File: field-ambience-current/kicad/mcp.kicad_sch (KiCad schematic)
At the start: 41 parts, among them SW1 Cell 1 (2u Choc V2 Hot-Swap), SW10 Modifier CLEAR (12x12x7.3 SMD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, SW2 Cell 2 (2u Choc V2 Hot-Swap), SW3 Cell 3 (2u Choc V2 Hot-Swap), SW4 Cell 4 (2u Choc V2 Hot-Swap), SW5 Cell 5 (2u Choc V2 Hot-Swap), SW6 Modifier SHIFT (12x12x7.3 SMD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, SW7 Modifier HOLD (12x12x7.3 SMD-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, SW8 Modifier DRONE (12x12x7.3 SMD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, SW9 Modifier GENERATE (12x12x7.3 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

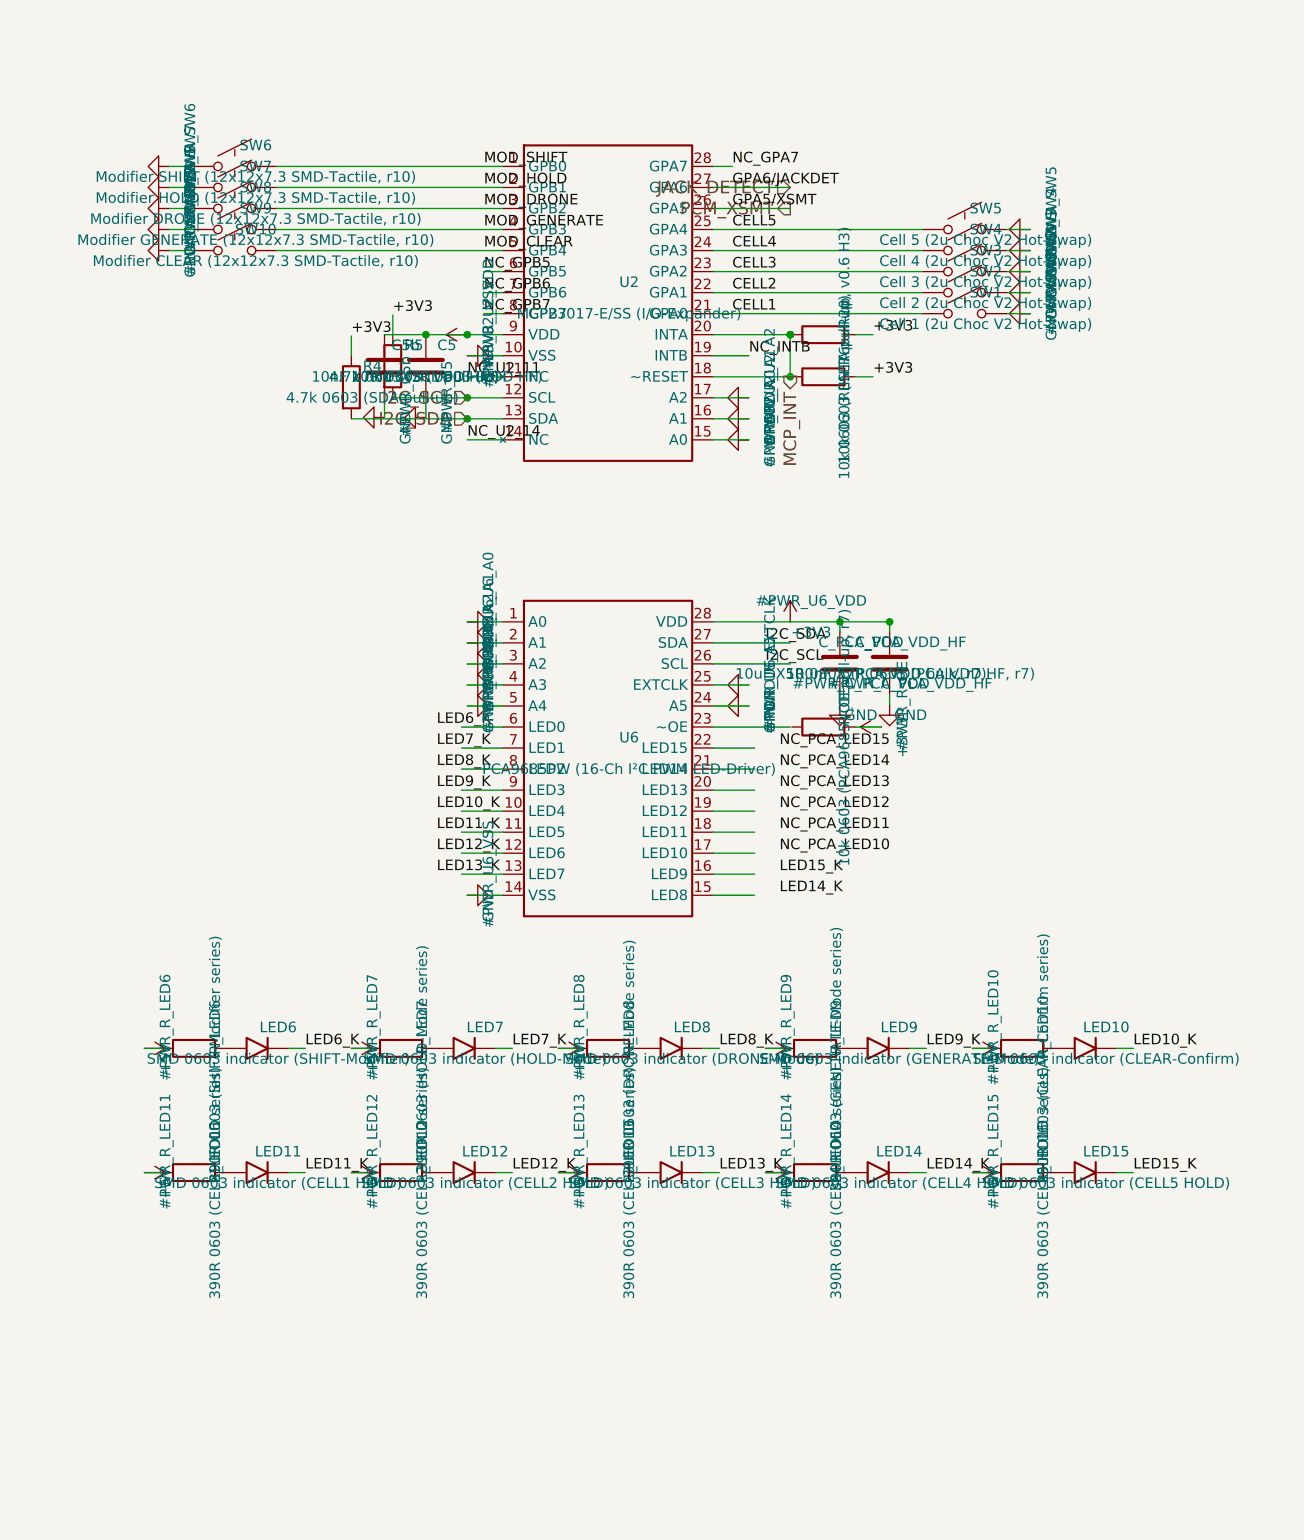
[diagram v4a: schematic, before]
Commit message: pcb(gen): r12-Sense + r9-Battery — KiCad-Generator vervollständigt
Zweite + dritte Hälfte von r10-B9/r7-B3. Bringt Generator vollständig in
Sync mit allen SPEC-Revisionen r9 (Battery-Add), r12 (Battery-Sense-HW),
r10-LED (LED1 auf PCA-Ch 10).

5 neue Library-Symbole (zwischen _pca9685pw_lib_symbol und
_rotary_encoder_switch_lib_symbol):
- _mcp73831_lib_symbol() — SOT-23-5, 5-pin Microchip-Charger
- _tps61089_lib_symbol() — QFN-12+ePAD, 13-pin TI-Boost
- _dmg2305ux_lib_symbol() — SOT-23, 3-pin P-MOSFET
- _inductor_lib_symbol() — Device:L, 2-pin
- _schottky_diode_lib_symbol() — Device:D_Schottky, 2-pin

Neuer Sheet 7 battery.kicad_sch (106 KB, 1848 Zeilen, paren-balanced):
- U7 MCP73831 LiPo-Charger 500mA via R21=2kΩ R_PROG, STAT→R_CHRG→LED_CHRG→+5V
- U8 TPS61089 Boost LiPo→5V mit L1 2.2µH + R23/R24 FB-Divider (200k/39k → ~4.92V)
- Q1 DMG2305UX P-MOS Power-Path (S=VBUS_USBC, D=+5V_OUT, G→R22 10kΩ pull-down)
- D3 SS34 Schottky zwischen BOOST_OUT und +5V_OUT (Reverse-Protect)
- J9 JST-PH-2P, C_BAT_IN/HF (22µF+100nF), C_BOOST_OUT/HF (22µF+100nF)
- Hier-I/O: VBUS_USBC ← (Power-Tree), BAT_PLUS → (Pico), +5V_OUT → (System-Rail)

r12-Sense in pico_sheet:
- GP26 STATUS_LED-Block entfernt (R19+LED1+GND-Flag weg, 0 hits in pico.kicad_sch)
- BAT_SENSE-Divider rein: R_BAT_DIV_TOP/BOT (100kΩ je), C_BAT_FILT (10nF)
- Hier-Input BAT_PLUS am Divider-Top

r12-Sense in mcp_sheet:
- GPA7 NC_GPA7 → USB_VBUS_SENSE mit R_VBUS_SENSE (10kΩ Series) + R_VBUS_PD
  (100kΩ Pull-Down) + hier-Input VBUS_USBC
- LED1 + R_LED_STATUS (390Ω 0603) auf PCA-Ch 10 (Pin 17, rechts) bei (130, 230)
- STATUS_LED_K Net-Label matched LED1-Kathode mit PCA-LED10-Pin
- NC-Loop reduziert auf LED11-LED15

power_tree_sheet:
- VBUS_USBC hier-Output (90° nach oben) am pre-fuse Rail-Tap bei (30.48, RAIL_Y-6)

root_sheet:
- Sheet 7 Battery-Block bei (30, 180) size 60×40 mit Pins VBUS_USBC/BAT_PLUS/+5V_OUT
- Existing Sheet-Blöcke erweitert: power_tree +VBUS_USBC out (90,95), pico +BAT_PLUS
  in (130,165), mcp +VBUS_USBC in 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
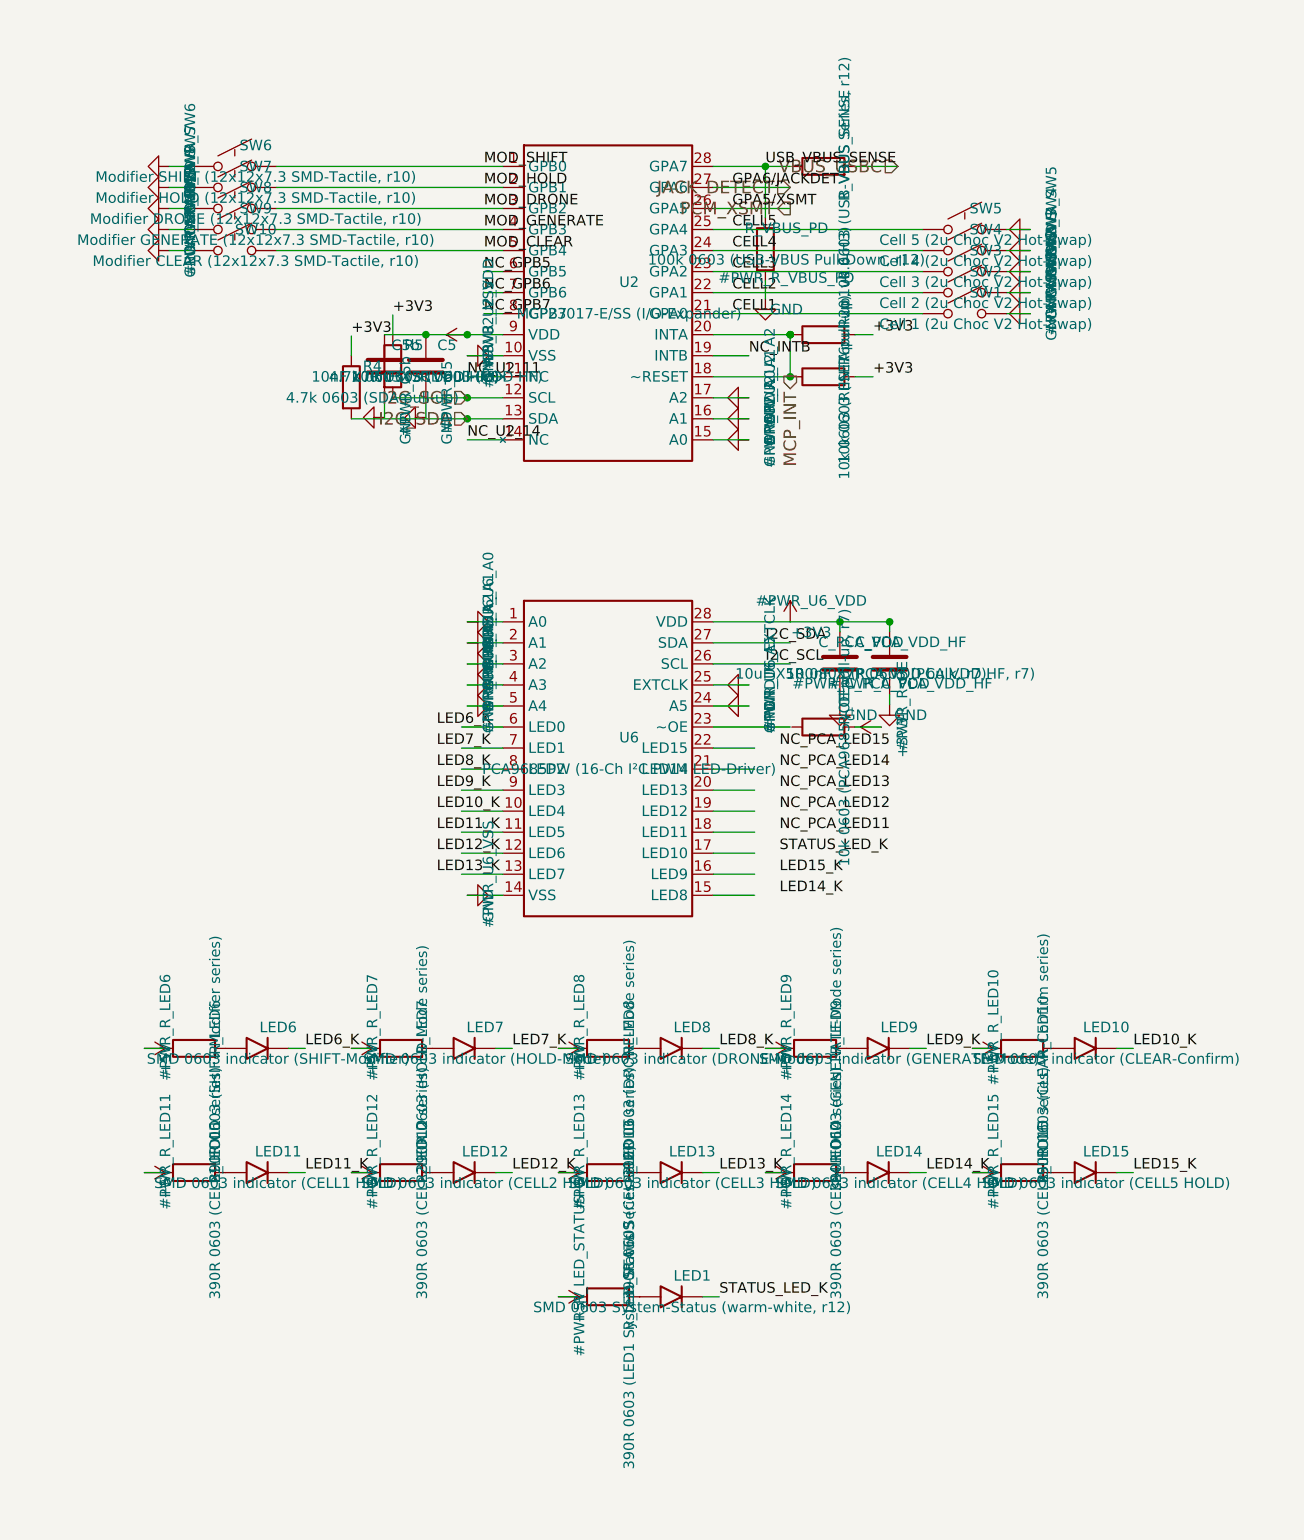
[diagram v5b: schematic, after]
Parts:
- added LED1: SMD 0603 System-Status (warm-white, r12), LED_SMD:LED_0603_1608Metric, symbol Device:LED
- added R_LED_STATUS: 390R 0603 (LED1 System-Status Series, r12), Resistor_SMD:R_0603_1608Metric, symbol Device:R
- added R_VBUS_PD: 100k 0603 (USB-VBUS Pull-Down, r12), Resistor_SMD:R_0603_1608Metric, symbol Device:R
- added R_VBUS_SENSE: 10k 0603 (USB-VBUS Series, r12), Resistor_SMD:R_0603_1608Metric, symbol Device:R
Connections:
- net +5V: now also R_LED_STATUS.1
- net GND: now also R_VBUS_PD.2
- net NC_GPA7 renamed USB_VBUS_SENSE
- net USB_VBUS_SENSE: now also R_VBUS_PD.1
- new net: LED1.2 (A), R_LED_STATUS.2
- new net STATUS_LED_K: LED1.1 (K)
- new net VBUS_USBC: R_VBUS_SENSE.2
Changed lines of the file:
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@@
       (project "field_ambience"
         (path "/ae4d8abd-ab57-48bd-a18a-f37b38917ad2" (reference "#PWR_SW10") (unit 1)))))
+  (symbol (lib_id "Device:R") (at 156 93.49 90) (unit 1)
+    (in_bom yes) (on_board yes) (dnp no)
+      (property "Reference" "R_VBUS_SENSE" (at 158.54 90.94999999999999 0)
+        (effects (font (size 1.27 1.27))))
+      (property "Value" "10k 0603 (USB-VBUS Series, r12)" (at 158.54 94.75999999999999 0)
+        (effects (font (size 1.27 1.27))))
+      (property "Footprint" "Resistor_SMD:R_0603_1608Metric" (at 156 93.49 0)
+        (effects (font (size 1.27 1.27)) hide))
+      (property "Datasheet" "~" (at 156 93.49 0)
+        (effects (font (size 1.27 1.27)) hide))
+      (property "MPN" "0603WAF1002T5E" (at 158.54 97.3 0)
+        (effects (font (size 1.27 1.27)) hide))
+      (property "LCSC" "C25804" (at 158.54 98.57 0)
+        (effects (font (size 1.27 1.27)) hide))
+    (instances
+      (project "field_ambience"
+        (path "/ae4d8abd-ab57-48bd-a18a-f37b38917ad2" (reference "R_VBUS_SENSE") (unit 1)))))
+  (symbol (lib_id "Device:R") (at 149 103.49 0) (unit 1)
+    (in_bom yes) (on_board yes) (dnp no)
+      (property "Reference" "R_VBUS_PD" (at 151.54 100.94999999999999 0)
+        (effects (font (size 1.27 1.27))))
+      (property "Value" "100k 0603 (USB-VBUS Pull-Down, r12)" (at 151.54 104.75999999999999 0)
+        (effects (font (size 1.27 1.27))))
+      (property "Footprint" "Resistor_SMD:R_0603_1608Metric" (at 149 103.49 0)
+        (effects (font (size 1.27 1.27)) hide))
+      (property "Datasheet" "~" (at 149 103.49 0)
+        (effects (font (size 1.27 1.27)) hide))
+      (property "MPN" "0603WAF1003T5E" (at 151.54 107.3 0)
+        (effects (font (size 1.27 1.27)) hide))
+      (property "LCSC" "C22796" (at 151.54 108.57 0)
+        (effects (font (size 1.27 1.27)) hide))
+    (instances
+      (project "field_ambience"
+        (path "/ae4d8abd-ab57-48bd-a18a-f37b38917ad2" (reference "R_VBUS_PD") (unit 1)))))
+  (symbol (lib_id "Power:GND") (at 149 109.49 0) (unit 1)
+    (in_bom yes) (on_board yes) (dnp no)
+      (property "Reference" "#PWR_R_VBUS_PD" (at 151.54 106.94999999999999 0)
+        (effects (font (size 1.27 1.27))))
+      (property "Value" "GND" (at 151.54 110.75999999999999 0)
+        (effects (font (size 1.27 1.27))))
+      (property "Footprint" "" (at 149 109.49 0)
+        (effects (font (size 1.27 1.27)) hide))
+      (property "Datasheet" "~" (at 149 109.49 0)
+        (effects (font (size 1.27 1.27)) hide))
+    (instances
+      (project "field_ambience"
+        (path "/ae4d8abd-ab57-48bd-a18a-f37b38917ad2" (reference "#PWR_R_VBUS_PD") (unit 1)))))
   (symbol (lib_id "Driver_LED:PCA9685PW") (at 130.0 165.0 0) (unit 1)
     (in_bom yes) (on_board yes) (dnp no)
@@
       (project "field_ambience"
         (path "/ae4d8abd-ab57-48bd-a18a-f37b38917ad2" (reference "LED15") (unit 1)))))
+  (symbol (lib_id "Device:R") (at 130.0 230.0 90) (unit 1)
+    (in_bom yes) (on_board yes) (dnp no)
+      (property "Reference" "R_LED_STATUS" (at 132.54 227.46 0)
+        (effects (font (size 1.27 1.27))))
+      (property "Value" "390R 0603 (LED1 System-Status Series, r12)" (at 132.54 231.27 0)
+        (effects (font (size 1.27 1.27))))
+      (property "Footprint" "Resistor_SMD:R_0603_1608Metric" (at 130.0 230.0 0)
+        (effects (font (size 1.27 1.27)) hide))
+      (property "Datasheet" "~" (at 130.0 230.0 0)
+        (effects (font (size 1.27 1.27)) hide))
+      (property "MPN" "0603WAF3900T5E" (at 132.54 233.81 0)
+        (effects (font (size 1.27 1.27)) hide))
+      (property "LCSC" "C23289" (at 132.54 235.08 0)
+        (effects (font (size 1.27 1.27)) hide))
+    (instances
+      (project "field_ambience"
+        (path "/ae4d8abd-ab57-48bd-a18a-f37b38917ad2" (reference "R_LED_STATUS") (unit 1)))))
+  (symbol (lib_id "Power:+5V") (at 124.0 230.0 270) (unit 1)
+    (in_bom yes) (on_board yes) (dnp no)
+      (property "Reference" "#PWR_R_LED_STATUS" (at 126.54 227.46 0)
+        (effects (font (size 1.27 1.27))))
+      (property "Value" "+5V" (at 126.54 231.27 0)
+        (effects (font (size 1.27 1.27))))
+      (property "Footprint" "" (at 124.0 230.0 0)
+        (effects (font (size 1.27 1.27)) hide))
+      (property "Datasheet" "~" (at 124.0 230.0 0)
+        (effects (font (size 1.27 1.27)) hide))
+    (instances
+      (project "field_ambience"
+        (path "/ae4d8abd-ab57-48bd-a18a-f37b38917ad2" (reference "#PWR_R_LED_STATUS") (unit 1)))))
+  (symbol (lib_id "Device:LED") (at 137.62 230.0 180) (unit 1)
+    (in_bom yes) (on_board yes) (dnp no)
+      (property "Reference" "LED1" (at 140.16 227.46 0)
+        (effects (font (size 1.27 1.27))))
+      (property "Value" "SMD 0603 System-Status (warm-white, r12)" (at 140.16 231.27 0)
+        (effects (font (size 1.27 1.27))))
+      (property "Footprint" "LED_SMD:LED_0603_1608Metric" (at 137.62 230.0 0)
+        (effects (font (size 1.27 1.27)) hide))
+      (property "Datasheet" "~" (at 137.62 230.0 0)
+        (effects (font (size 1.27 1.27)) hide))
+      (property "MPN" "Generic warm-white 0603" (at 140.16 233.81 0)
+        (effects (font (size 1.27 1.27)) hide))
+      (property "LCSC" "C72043" (at 140.16 235.08 0)
+        (effects (font (size 1.27 1.27)) hide))
+    (instances
+      (project "field_ambience"
+        (path "/ae4d8abd-ab57-48bd-a18a-f37b38917ad2" (reference "LED1") (unit 1)))))
   (wire (pts (xy 142.7 126.50999999999999) (xy 147 126.50999999999999))
     (stroke (width 0) (type default))
@@
     (stroke (width 0) (type default))
 )
-  (wire (pts (xy 142.7 93.49) (xy 145 93.49))
+  (wire (pts (xy 142.7 93.49) (xy 152 93.49))
+    (stroke (width 0) (type default))
+)
+  (wire (pts (xy 159.81 93.49) (xy 165 93.49))
+    (stroke (width 0) (type default))
+)
+  (wire (pts (xy 149 93.49) (xy 149 99.67999999999999))
+    (stroke (width 0) (type default))
+)
+  (wire (pts (xy 149 107.3) (xy 149 109.49))
     (stroke (width 0) (type default))
 )
@@
     (stroke (width 0) (type default))
 )
+  (wire (pts (xy 126.19 230.0) (xy 124.0 230.0))
+    (stroke (width 0) (type default))
+)
+  (wire (pts (xy 141.43 230.0) (xy 143.43 230.0))
+    (stroke (width 0) (type default))
+)
   (junction (at 113 113.81) (diameter 0) (color 0 0 0 0)
 )
@@
   (junction (at 152 113.81) (diameter 0) (color 0 0 0 0)
 )
+  (junction (at 149 93.49) (diameter 0) (color 0 0 0 0)
+)
   (junction (at 158 148.49) (diameter 0) (color 0 0 0 0)
 )
@@
     (effects (font (size 1.27 1.27)) (justify left bottom))
 )
-  (label "NC_GPA7" (at 145 93.49 0) (fields_autoplaced)
+  (label "USB_VBUS_SENSE" (at 149 93.49 0) (fields_autoplaced)
     (effects (font (size 1.27 1.27)) (justify left bottom))
 )
@@
     (effects (font (size 1.27 1.27)) (justify left bottom))
 )
-  (label "NC_PCA_LED10" (at 150.7 176.43 0) (fields_autoplaced)
+  (label "STATUS_LED_K" (at 150.7 176.43 0) (fields_autoplaced)
     (effects (font (size 1.27 1.27)) (justify left bottom))
 )
@@
 )
   (label "NC_PCA_LED15" (at 150.7 163.73000000000002 0) (fields_autoplaced)
+    (effects (font (size 1.27 1.27)) (justify left bottom))
+)
+  (label "STATUS_LED_K" (at 143.43 230.0 0) (fields_autoplaced)
     (effects (font (size 1.27 1.27)) (justify left bottom))
 )
@@
     (effects (font (size 1.524 1.524)) (justify right))
 )
+  (hierarchical_label "VBUS_USBC" (shape input) (at 165 93.49 180)
+    (effects (font (size 1.524 1.524)) (justify right))
+)
